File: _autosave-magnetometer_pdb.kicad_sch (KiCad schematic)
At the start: 59 parts, among them J1 Screw_Terminal_01x02, J10 Screw_Terminal_01x02, J11 Screw_Terminal_01x02, J12 Screw_Terminal_01x02, J13 Screw_Terminal_01x02, J14 Screw_Terminal_01x02, J2 Screw_Terminal_01x02, J3 Screw_Terminal_01x02, J4 Screw_Terminal_01x02, J6 Conn_01x02_Pin, J7 Conn_01x02_Pin, J8 Conn_01x02_Pin, J9 Screw_Terminal_01x02, U2 L78L09_SO8, U3 ${SIM.PARAMS}, U4 ${SIM.PARAMS}, U5 ${SIM.PARAMS}, U6 ${SIM.PARAMS}

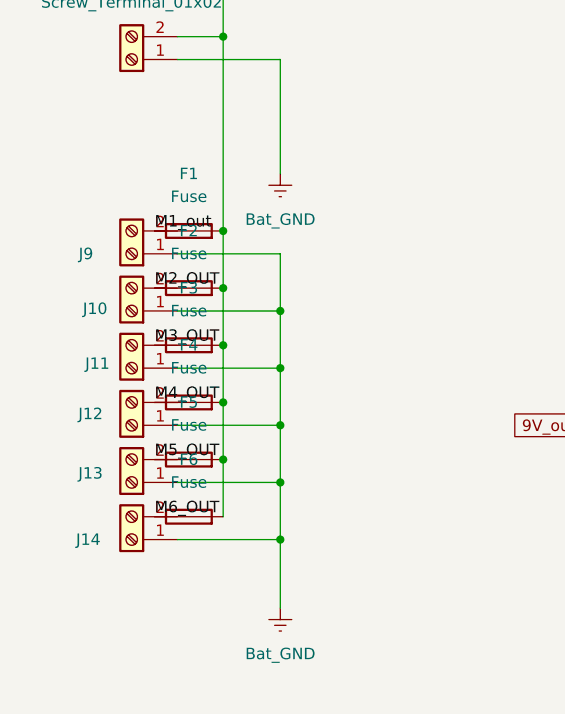
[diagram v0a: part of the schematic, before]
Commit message: Cleaned up PCB and added Fuses
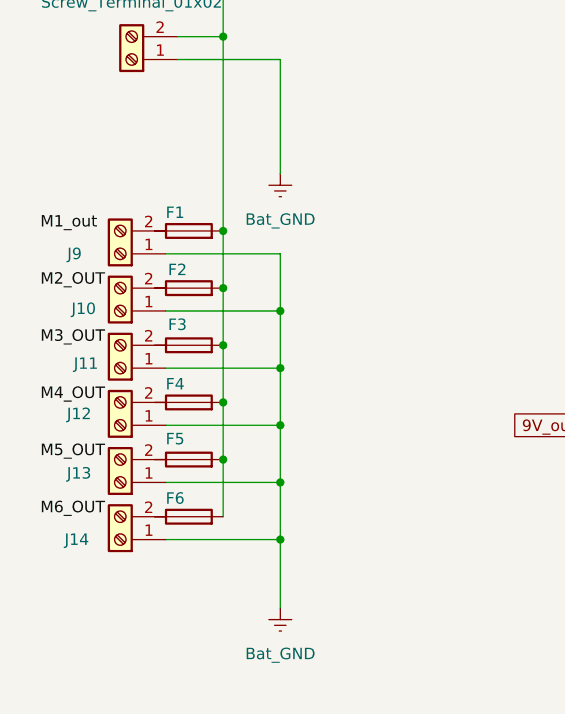
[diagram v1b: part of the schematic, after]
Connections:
- net M1_out: no longer F1.1
- net M2_OUT: no longer F2.1
- net M3_OUT: no longer F3.1
- net M4_OUT: no longer F4.1
- net M5_OUT: no longer F5.1
- net M6_OUT: no longer F6.1
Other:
- moved on the sheet: J10, J11, J12, J13, J14, J9
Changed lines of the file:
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@@
 	(wire
 		(pts
-			(xy 27.94 120.65) (xy 39.37 120.65)
+			(xy 26.67 120.65) (xy 39.37 120.65)
 		)
 		(stroke
@@
 	(wire
 		(pts
-			(xy 27.94 107.95) (xy 39.37 107.95)
+			(xy 26.67 107.95) (xy 39.37 107.95)
 		)
 		(stroke
@@
 	(wire
 		(pts
-			(xy 27.94 127) (xy 39.37 127)
+			(xy 26.67 127) (xy 39.37 127)
 		)
 		(stroke
@@
 	(wire
 		(pts
-			(xy 27.94 95.25) (xy 39.37 95.25)
+			(xy 26.67 95.25) (xy 39.37 95.25)
 		)
 		(stroke
@@
 	(wire
 		(pts
-			(xy 27.94 114.3) (xy 39.37 114.3)
+			(xy 26.67 114.3) (xy 39.37 114.3)
 		)
 		(stroke
@@
 	(wire
 		(pts
-			(xy 27.94 101.6) (xy 39.37 101.6)
+			(xy 26.67 101.6) (xy 39.37 101.6)
 		)
 		(stroke
@@
 	)
 	(label "M2_OUT"
-		(at 25.4 99.06 0)
+		(at 12.7 99.06 0)
 		(effects
 			(font
@@
 	)
 	(label "M3_OUT"
-		(at 25.4 105.41 0)
+		(at 12.7 105.41 0)
 		(effects
 			(font
@@
 	)
 	(label "M5_OUT"
-		(at 25.4 118.11 0)
+		(at 12.7 118.11 0)
 		(effects
 			(font
@@
 	)
 	(label "M4_OUT"
-		(at 25.4 111.76 0)
+		(at 12.7 111.76 0)
 		(effects
 			(font
@@
 	)
 	(label "M6_OUT"
-		(at 25.4 124.46 0)
+		(at 12.7 124.46 0)
 		(effects
 			(font
@@
 	)
 	(label "M1_out"
-		(at 25.4 92.71 0)
+		(at 12.7 92.71 0)
 		(effects
 			(font
@@
 		(polyline
 			(pts
-				(xy 147.32 25.4) (xy 147.32 163.83) (xy 266.7 165.1) (xy 266.7 25.4) (xy 266.7 25.4)
+				(xy 29.21 13.97) (xy 138.43 13.97) (xy 138.43 194.31) (xy 29.21 194.31) (xy 29.21 190.5)
 			)
 			(stroke
 				(width 0)
 				(type dash)
+				(color 0 194 0 1)
 			)
 			(fill
 				(type color)
-				(color 194 0 194 0.14)
+				(color 0 255 0 0.2)
 			)
 		)
@@
 		(polyline
 			(pts
-				(xy 29.21 13.97) (xy 138.43 13.97) (xy 138.43 194.31) (xy 29.21 194.31) (xy 29.21 190.5)
+				(xy 147.32 25.4) (xy 147.32 163.83) (xy 266.7 165.1) (xy 266.7 25.4) (xy 266.7 25.4)
 			)
 			(stroke
 				(width 0)
 				(type dash)
-				(color 0 194 0 1)
 			)
 			(fill
 				(type color)
-				(color 0 255 0 0.2)
+				(color 194 0 194 0.14)
 			)
 		)
@@
 	(symbol
 		(lib_id "Connector:Screw_Terminal_01x02")
-		(at 22.86 107.95 180)
+		(at 21.59 107.95 180)
 		(unit 1)
 		(exclude_from_sim no)
@@
 		(dnp no)
 		(property "Reference" "J11"
-			(at 19.05 107.442 0)
+			(at 17.78 107.442 0)
 			(effects
 				(font
@@
 		)
 		(property "Value" "Screw_Terminal_01x02"
-			(at 22.86 101.6 0)
+			(at 21.59 101.6 0)
 			(effects
 				(font
@@
 		)
 		(property "Footprint" "Connector_PinHeader_2.00mm:2_Pin_Screw_Term"
-			(at 22.86 107.95 0)
+			(at 21.59 107.95 0)
 			(effects
 				(font
@@
 		)
 		(property "Datasheet" "~"
-			(at 22.86 107.95 0)
+			(at 21.59 107.95 0)
 			(effects
 				(font
@@
 		)
 		(property "Description" "Generic screw terminal, single row, 01x02, script generated (kicad-library-utils/schlib/autogen/connector/)"
-			(at 22.86 107.95 0)
+			(at 21.59 107.95 0)
 			(effects
 				(font
@@
 		(on_board yes)
 		(dnp no)
-		(fields_autoplaced yes)
 		(property "Reference" "F5"
-			(at 29.21 111.76 90)
+			(at 27.686 115.824 90)
 			(effects
 				(font
@@
 					(size 1.27 1.27)
 				)
+				(hide yes)
 			)
 		)
@@
 	(symbol
 		(lib_id "Connector:Screw_Terminal_01x02")
-		(at 22.86 95.25 180)
+		(at 21.59 95.25 180)
 		(unit 1)
 		(exclude_from_sim no)
@@
 		(dnp no)
 		(property "Reference" "J9"
-			(at 17.78 95.25 0)
+			(at 16.51 95.25 0)
 			(effects
 				(font
@@
 		)
 		(property "Value" "Screw_Terminal_01x02"
-			(at 22.86 88.9 0)
+			(at 21.59 88.9 0)
 			(effects
 				(font
@@
 		)
 		(property "Footprint" "Connector_PinHeader_2.00mm:2_Pin_Screw_Term"
-			(at 22.86 95.25 0)
+			(at 21.59 95.25 0)
 			(effects
 				(font
@@
 		)
 		(property "Datasheet" "~"
-			(at 22.86 95.25 0)
+			(at 21.59 95.25 0)
 			(effects
 				(font
@@
 		)
 		(property "Description" "Generic screw terminal, single row, 01x02, script generated (kicad-library-utils/schlib/autogen/connector/)"
-			(at 22.86 95.25 0)
+			(at 21.59 95.25 0)
 			(effects
 				(font
@@
 		(on_board yes)
 		(dnp no)
-		(fields_autoplaced yes)
 		(property "Reference" "F6"
-			(at 29.21 118.11 90)
+			(at 27.686 122.428 90)
 			(effects
 				(font
@@
 					(size 1.27 1.27)
 				)
+				(hide yes)
 			)
 		)
@@
 		(on_board yes)
 		(dnp no)
-		(fields_autoplaced yes)
 		(property "Reference" "F2"
-			(at 29.21 92.71 90)
+			(at 27.94 97.028 90)
 			(effects
 				(font
@@
 					(size 1.27 1.27)
 				)
+				(hide yes)
 			)
 		)
@@
 	(symbol
 		(lib_id "Connector:Screw_Terminal_01x02")
-		(at 22.86 101.6 180)
+		(at 21.59 101.6 180)
 		(unit 1)
 		(exclude_from_sim no)
@@
 		(dnp no)
 		(property "Reference" "J10"
-			(at 18.796 101.346 0)
+			(at 17.526 101.346 0)
 			(effects
 				(font
@@
 		)
 		(property "Value" "Screw_Terminal_01x02"
-			(at 22.86 95.25 0)
+			(at 21.59 95.25 0)
 			(effects
 				(font
@@
 		)
 		(property "Footprint" "Connector_PinHeader_2.00mm:2_Pin_Screw_Term"
-			(at 22.86 101.6 0)
+			(at 21.59 101.6 0)
 			(effects
 				(font
@@
 		)
 		(property "Datasheet" "~"
-			(at 22.86 101.6 0)
+			(at 21.59 101.6 0)
 			(effects
 				(font
@@
 		)
 		(property "Description" "Generic screw terminal, single row, 01x02, script generated (kicad-library-utils/schlib/autogen/connector/)"
-			(at 22.86 101.6 0)
+			(at 21.59 101.6 0)
 			(effects
 				(font
@@
 		(dnp no)
 		(property "Reference" "F3"
-			(at 29.21 99.06 90)
+			(at 27.94 103.124 90)
 			(effects
 				(font
@@
 					(size 1.27 1.27)
 				)
+				(hide yes)
 			)
 		)
@@
 	)
 	(symbol
+		(lib_name "Fuse_1")
 		(lib_id "Device:Fuse")
 		(at 29.21 92.71 90)
@@
 		(on_board yes)
 		(dnp no)
-		(fields_autoplaced yes)
 		(property "Reference" "F1"
-			(at 29.21 86.36 90)
+			(at 27.686 90.678 90)
 			(effects
 				(font
@@
 					(size 1.27 1.27)
 				)
+				(hide yes)
 			)
 		)
@@
 	(symbol
 		(lib_id "Connector:Screw_Terminal_01x02")
-		(at 22.86 114.3 180)
+		(at 21.59 114.3 180)
 		(unit 1)
 		(exclude_from_sim no)
@@
 		(dnp no)
 		(property "Reference" "J12"
-			(at 18.288 113.03 0)
+			(at 17.018 113.03 0)
 			(effects
 				(font
@@
 		)
 		(property "Value" "Screw_Terminal_01x02"
-			(at 22.86 107.95 0)
+			(at 21.59 107.95 0)
 			(effects
 				(font
@@
 		)
 		(property "Footprint" "Connector_PinHeader_2.00mm:2_Pin_Screw_Term"
-			(at 22.86 114.3 0)
+			(at 21.59 114.3 0)
 			(effects
 				(font
@@
 		)
 		(property "Datasheet" "~"
-			(at 22.86 114.3 0)
+			(at 21.59 114.3 0)
 			(effects
 				(font
@@
 		)
 		(property "Description" "Generic screw terminal, single row, 01x02, script generated (kicad-library-utils/schlib/autogen/connector/)"
-			(at 22.86 114.3 0)
+			(at 21.59 114.3 0)
 			(effects
 				(font
@@
 	(symbol
 		(lib_id "Connector:Screw_Terminal_01x02")
-		(at 22.86 127 180)
+		(at 21.59 127 180)
 		(unit 1)
 		(exclude_from_sim no)
@@
 		(dnp no)
 		(property "Reference" "J14"
-			(at 18.034 127 0)
+			(at 16.764 127 0)
 			(effects
 				(font
@@
 		)
 		(property "Value" "Screw_Terminal_01x02"
-			(at 27.178 131.572 0)
+			(at 25.908 131.572 0)
 			(effects
 				(font
@@
 		)
 		(property "Footprint" "Connector_PinHeader_2.00mm:2_Pin_Screw_Term"
-			(at 22.86 127 0)
+			(at 21.59 127 0)
 			(effects
 				(font
@@
 		)
 		(property "Datasheet" "~"
-			(at 22.86 127 0)
+			(at 21.59 127 0)
 			(effects
 				(font
@@
 		)
 		(property "Description" "Generic screw terminal, single row, 01x02, script generated (kicad-library-utils/schlib/autogen/connector/)"
-			(at 22.86 127 0)
+			(at 21.59 127 0)
 			(effects
 				(font
@@
 		(on_board yes)
 		(dnp no)
-		(fields_autoplaced yes)
 		(property "Reference" "F4"
-			(at 29.21 105.41 90)
+			(at 27.686 109.728 90)
 			(effects
 				(font
@@
 					(size 1.27 1.27)
 				)
+				(hide yes)
 			)
 		)
@@
 	(symbol
 		(lib_id "Connector:Screw_Terminal_01x02")
-		(at 22.86 120.65 180)
+		(at 21.59 120.65 180)
 		(unit 1)
 		(exclude_from_sim no)
@@
 		(dnp no)
 		(property "Reference" "J13"
-			(at 18.288 119.634 0)
+			(at 17.018 119.634 0)
 			(effects
 				(font
@@
 		)
 		(property "Value" "Screw_Terminal_01x02"
-			(at 22.86 114.3 0)
+			(at 21.59 114.3 0)
 			(effects
 				(font
@@
 		)
 		(property "Footprint" "Connector_PinHeader_2.00mm:2_Pin_Screw_Term"
-			(at 22.86 120.65 0)
+			(at 21.59 120.65 0)
 			(effects
 				(font
@@
 		)
 		(property "Datasheet" "~"
-			(at 22.86 120.65 0)
+			(at 21.59 120.65 0)
 			(effects
 				(font
@@
 		)
 		(property "Description" "Generic screw terminal, single row, 01x02, script generated (kicad-library-utils/schlib/autogen/connector/)"
-			(at 22.86 120.65 0)
+			(at 21.59 120.65 0)
 			(effects
 				(font
